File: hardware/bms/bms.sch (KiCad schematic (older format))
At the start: 159 parts

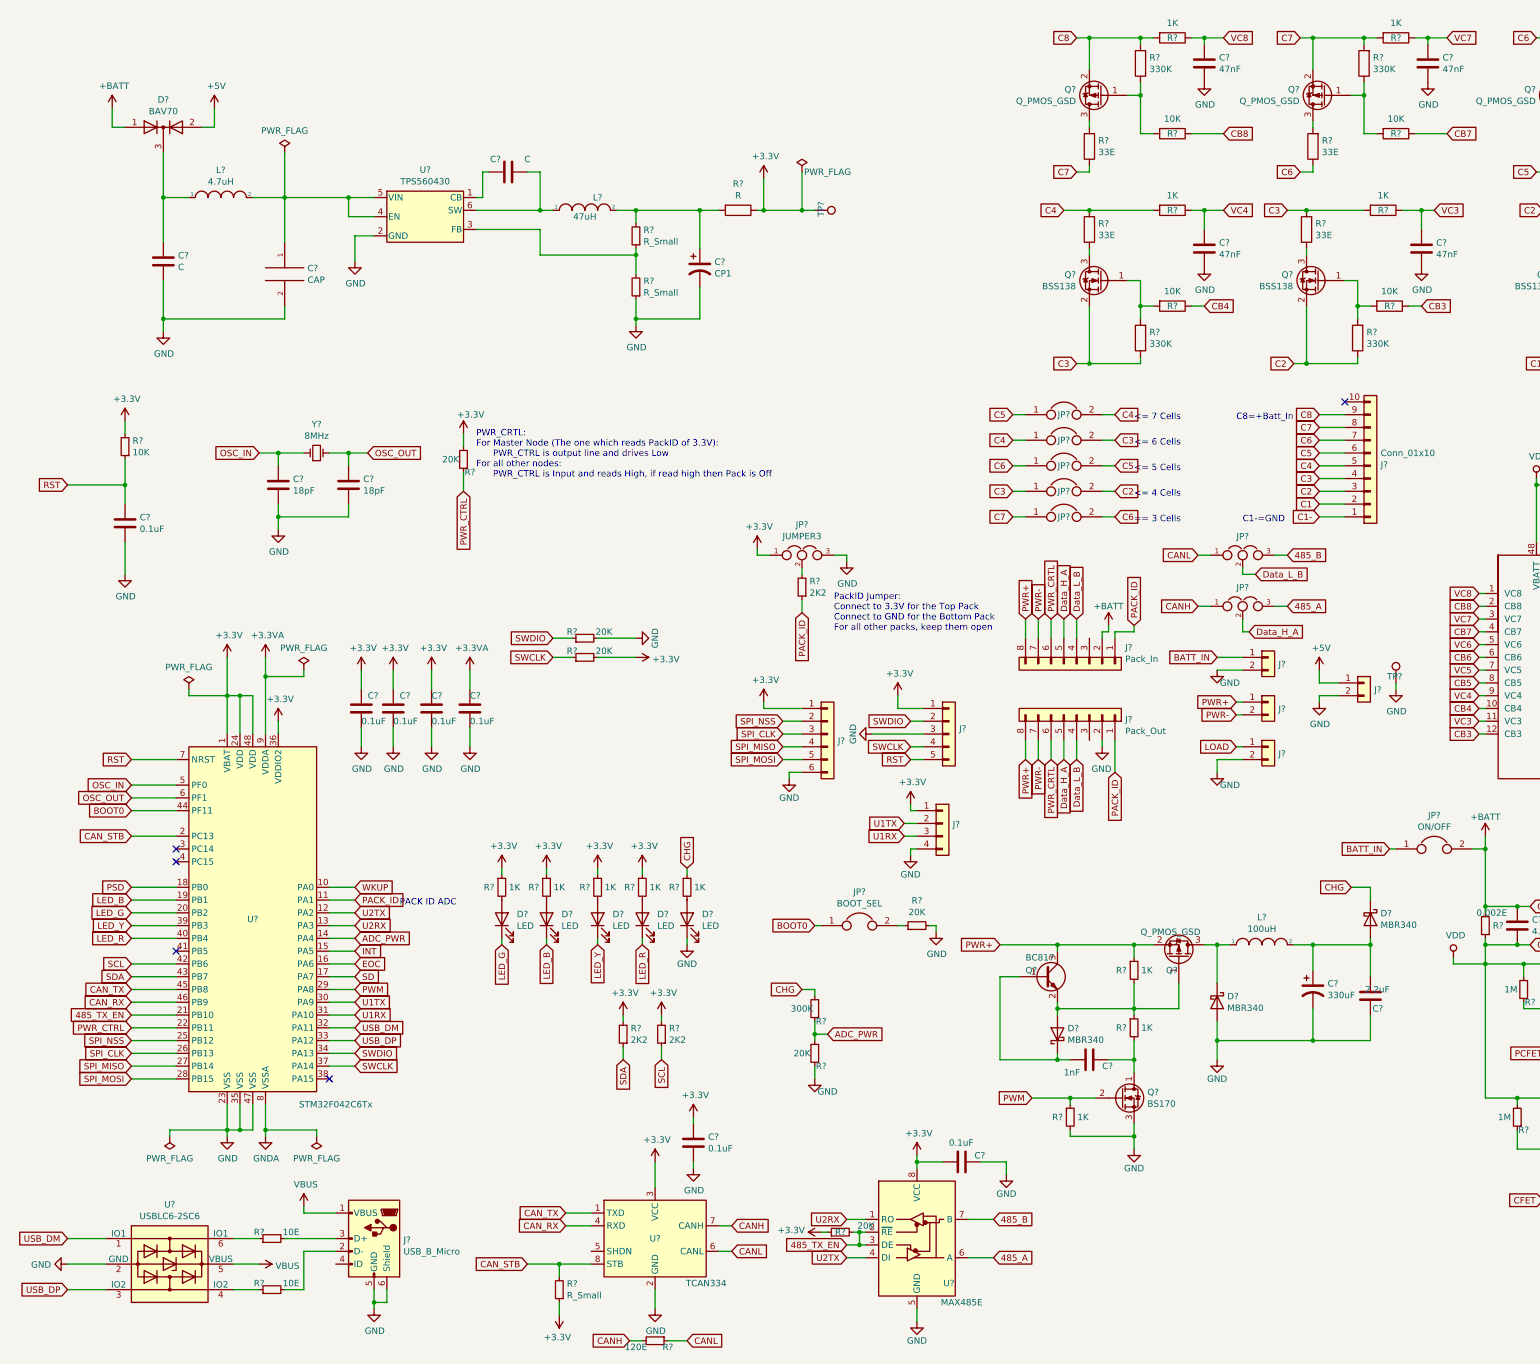
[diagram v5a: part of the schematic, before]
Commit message: added switching logic for gnd and chg control
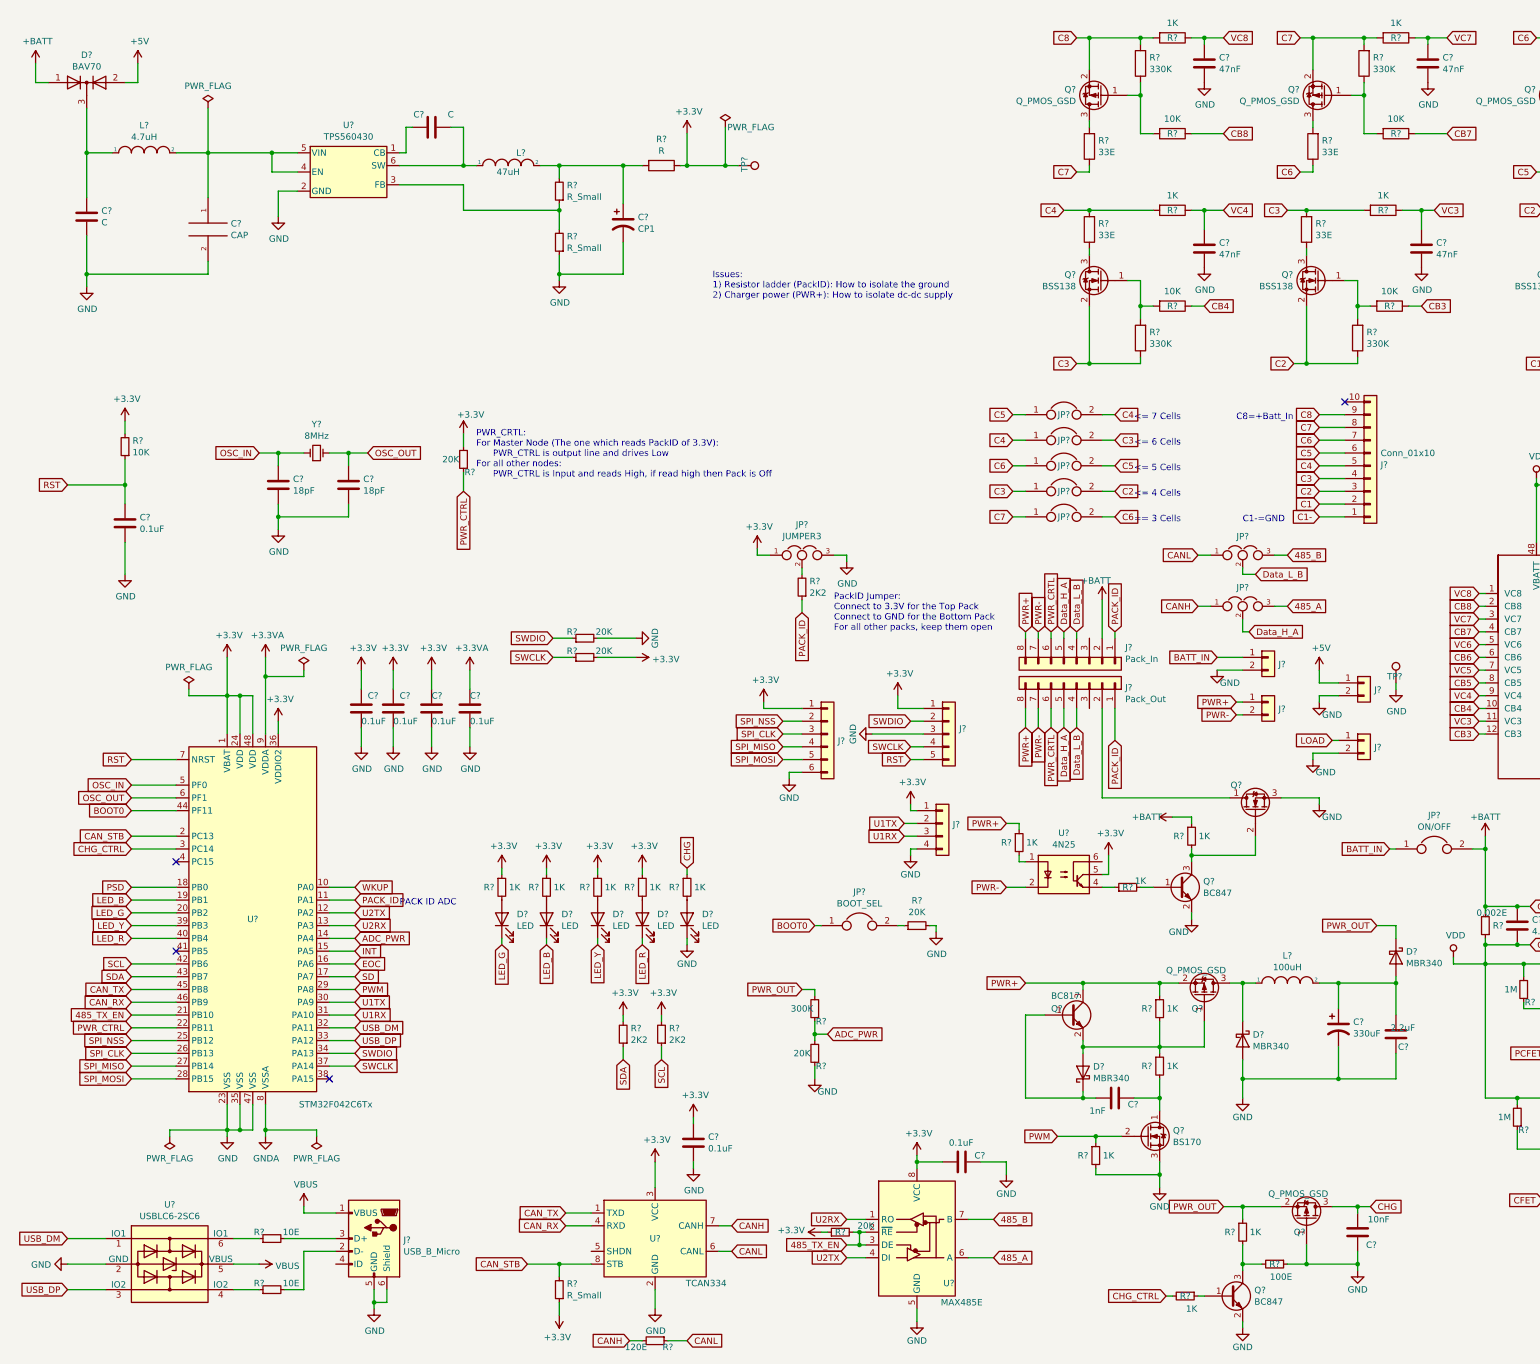
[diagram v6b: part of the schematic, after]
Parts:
- added C?: 10nF, Capacitor_SMD:C_0603_1608Metric_Pad1.05x0.95mm_HandSolder, symbol Device:C
- added Q?: Q_PMOS_GSD, symbol bms-rescue:Q_PMOS_GSD-BMS
- added Q? (x2): BC847, Package_TO_SOT_SMD:SOT-23, symbol Transistor_BJT:BC847
- added Q?: Q_NMOS_DGS, symbol Device:Q_NMOS_DGS
- added R? (x5): 1K, Resistor_SMD:R_0603_1608Metric_Pad1.05x0.95mm_HandSolder, symbol Device:R_Small
- added R?: 100E, Resistor_SMD:R_0603_1608Metric_Pad1.05x0.95mm_HandSolder, symbol Device:R_Small
- added U?: 4N25, Package_DIP:DIP-6_W7.62mm, symbol Isolator:4N25
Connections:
- net +3V3: now also U?.5
- net +BATT: now also R?.1
- net CHG: now also C?.2, Q?.3 (D); no longer D?.1 (K), R?.2
- net GND: now also C?.1, Q?.1 (G), Q?.2 (E), Q?.2 (E), Q?.3 (S), R?.1; no longer J?.2 (Pin_2)
- net PWR+: now also R?.1
- net PWR-: now also U?.2
- net CHG_CTRL: now reaches U?.3 (PC14)
- net CHG_CTRL: now also R?.2
- new net: Q?.1 (B), R?.1
- new net: Q?.3 (C), R?.2, R?.2
- new net: Q?.1 (B), R?.2
- new net: Q?.2 (G), Q?.3 (C), R?.2
- new net: R?.1, U?.4
- new net: J?.2 (Pin_2), Q?.1 (D)
- new net: R?.2, U?.1
- new net PWR_OUT: D?.1 (K), Q?.2 (S), R?.1, R?.2
- no-connect marks 7 -> 6
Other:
- note added: "Issues:\n1) Resistor ladder (PackID): How to isolate the ground\n2) Charger power (PWR+): How to isolate dc-dc supply"
- moved on the sheet: C?, D?, J?, L?, Q?, R?, TP?, U?

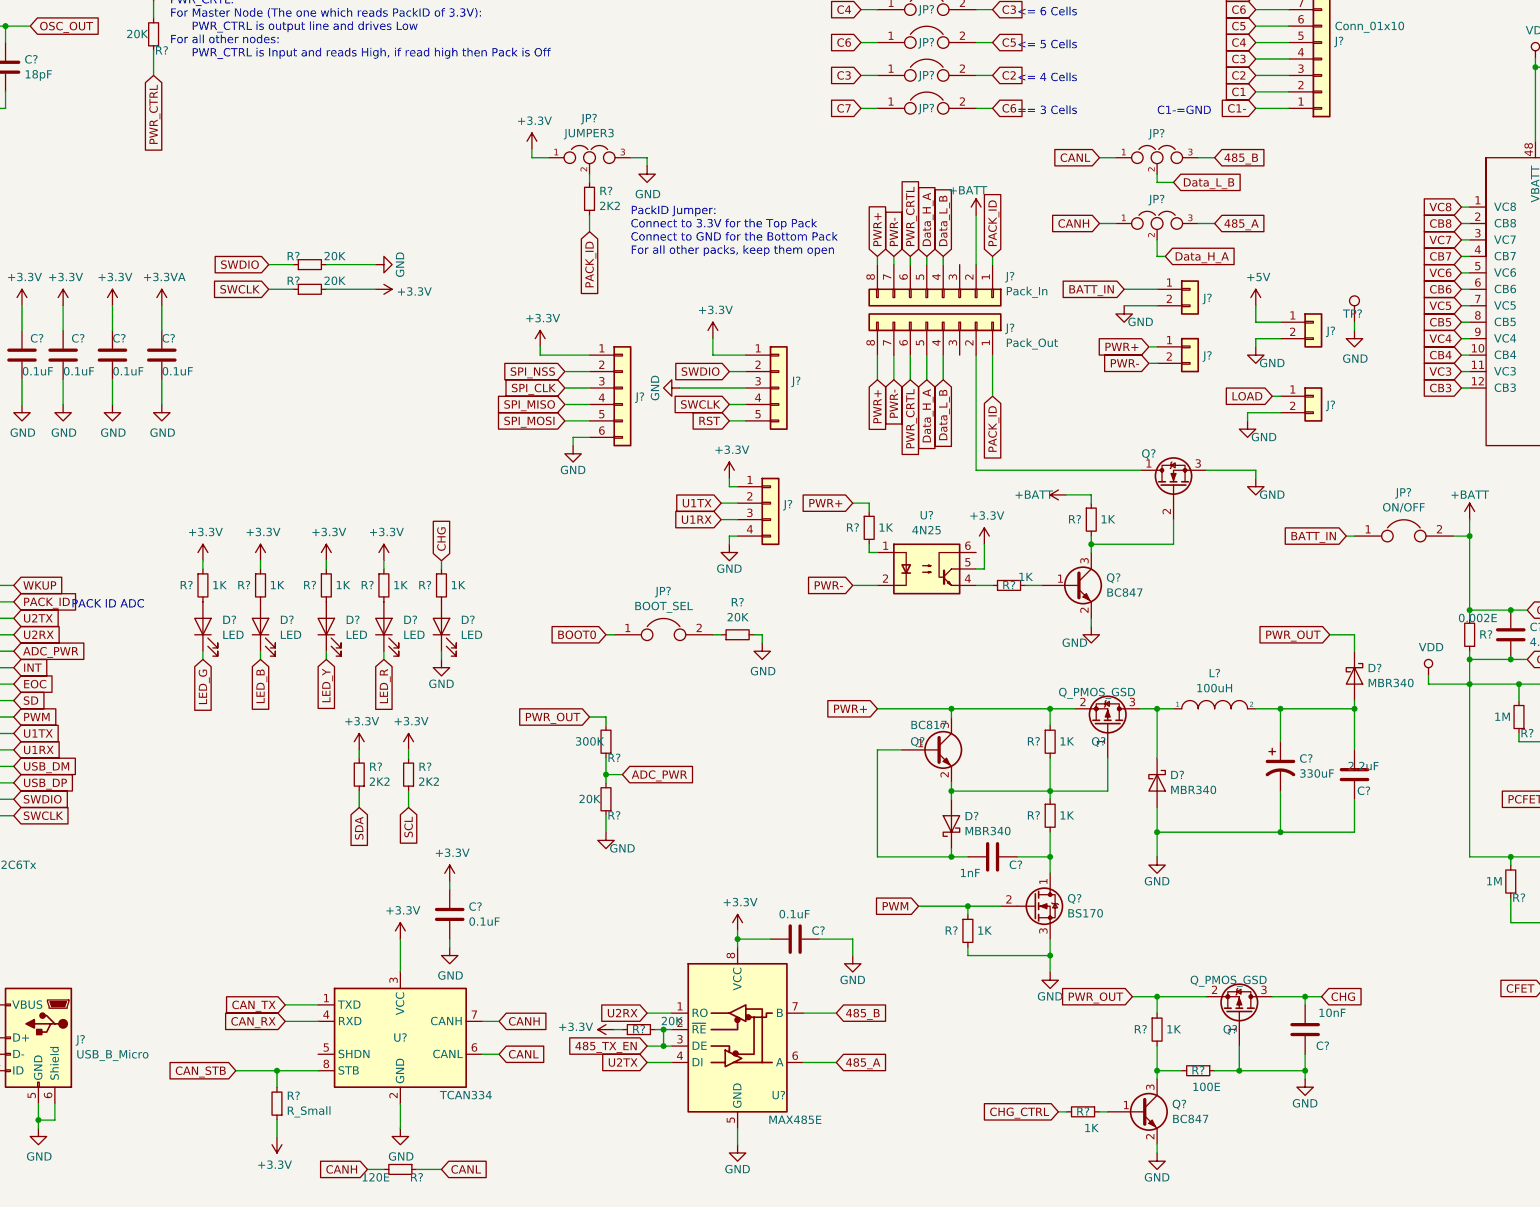
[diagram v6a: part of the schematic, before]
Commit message: updated charging logic and board to board connections
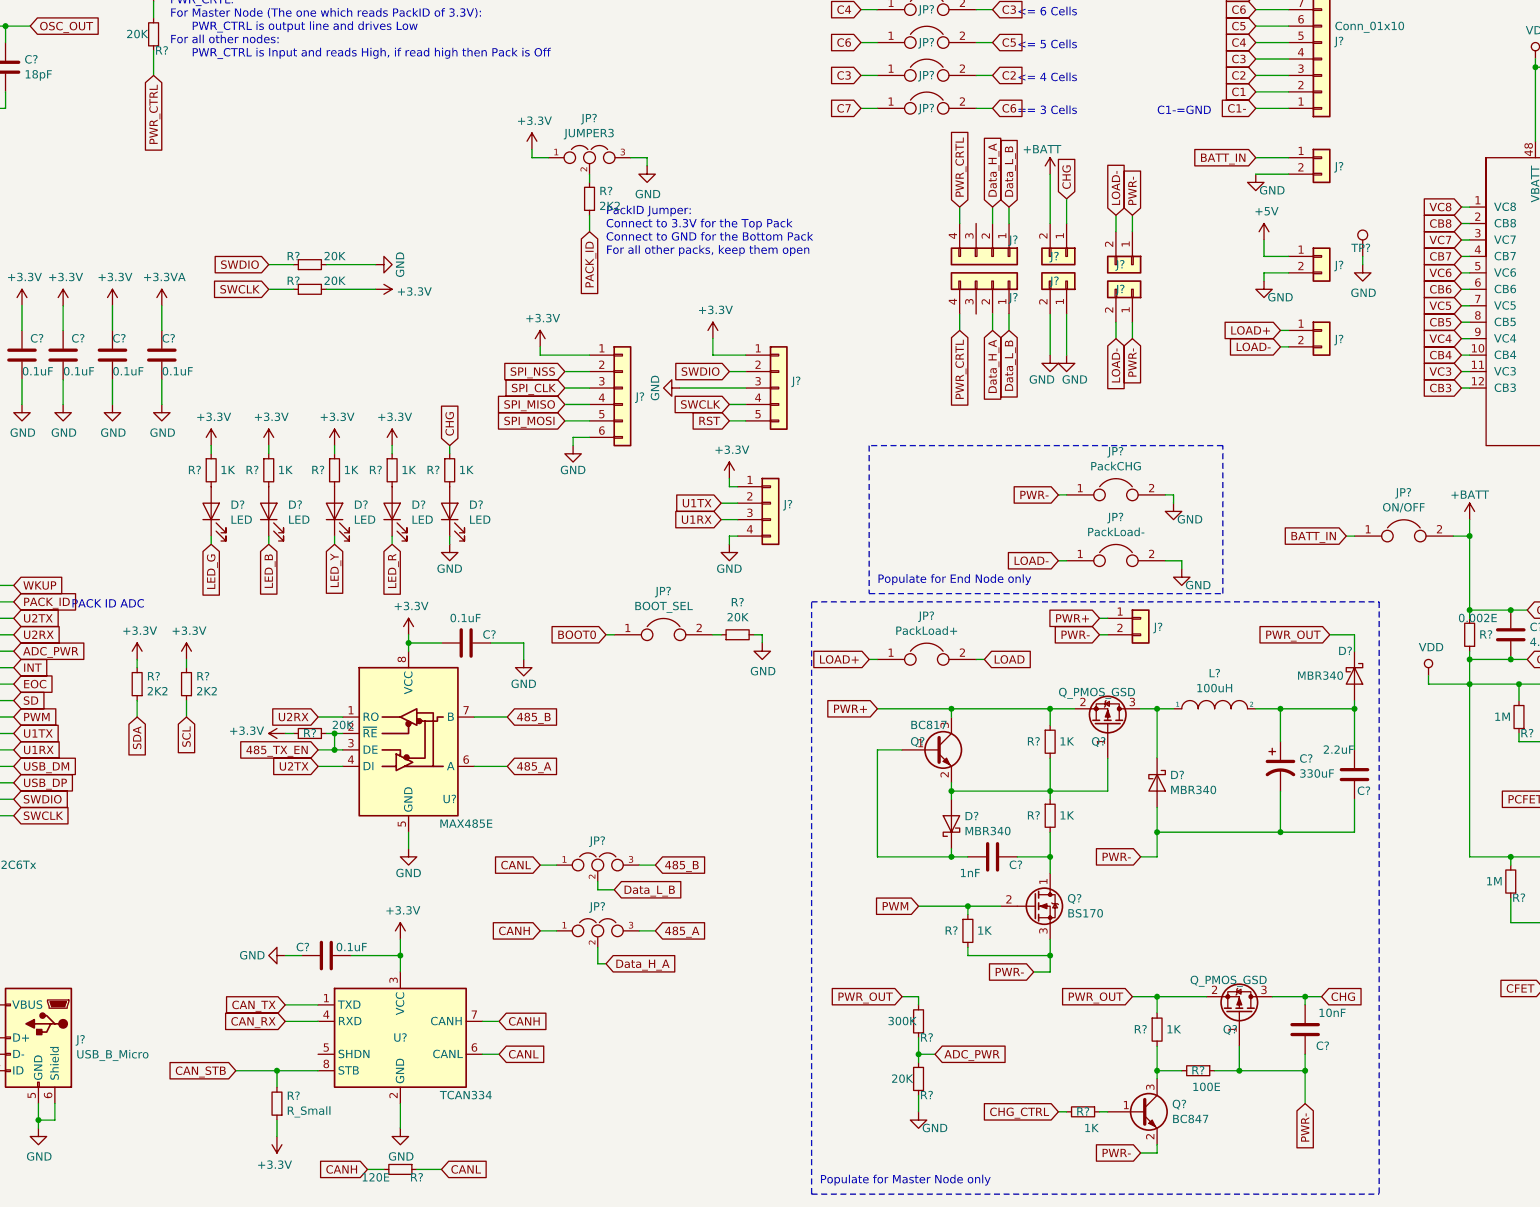
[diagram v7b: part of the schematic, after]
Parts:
- removed J?: Pack_In, symbol Connector_Generic:Conn_01x08
- removed J?: Pack_Out, symbol Connector_Generic:Conn_01x08
- removed Q?: BC847, Package_TO_SOT_SMD:SOT-23, symbol Transistor_BJT:BC847
- removed Q?: Q_NMOS_DGS, symbol Device:Q_NMOS_DGS
- removed R? (x3): 1K, Resistor_SMD:R_0603_1608Metric_Pad1.05x0.95mm_HandSolder, symbol Device:R_Small
- removed U?: 4N25, Package_DIP:DIP-6_W7.62mm, symbol Isolator:4N25
- added J? (x2): Conn_01x04, symbol Connector_Generic:Conn_01x04
- added J? (x4): Conn_01x02, symbol BMS:Conn_01x02
- added JP?: PackCHG, symbol BMS:JUMPER
- added JP?: PackLoad+, symbol BMS:JUMPER
- added JP?: PackLoad-, symbol BMS:JUMPER
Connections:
- net +3V3: now also C?.2; no longer C?.1
- net +BATT: now also J?.2 (Pin_2)
- net CHG: now also J?.1 (Pin_1)
- net Data_H_A: now also J?.2 (Pin_2), J?.2 (Pin_2)
- net Data_L_B: now also J?.1 (Pin_1), J?.1 (Pin_1)
- net GND: now also C?.1, J?.1 (Pin_1), J?.2 (Pin_2), JP?.2, JP?.2; no longer C?.1, C?.1, C?.2, C?.2, D?.2 (A), J?.2 (Pin_2), Q?.1 (G), Q?.2 (E), Q?.3 (S), R?.1, R?.2
- net LOAD: now also JP?.2; no longer J?.1 (Pin_1)
- net PWR-: now also C?.1, C?.1, C?.2, D?.2 (A), Q?.1 (G), Q?.2 (E), Q?.3 (S), R?.1, R?.2, J?.1 (Pin_1), J?.1 (Pin_1), JP?.1
- net PWR_CRTL: now also J?.4 (Pin_4), J?.4 (Pin_4)
- new net LOAD+: J?.1 (Pin_1), JP?.1
- new net LOAD-: J?.2 (Pin_2), J?.2 (Pin_2), J?.2 (Pin_2), JP?.1
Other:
- note added: "Populate for End Node only"
- note added: "Populate for Master Node only"
- moved on the sheet: C?, D?, J?, JP?, R?, TP?, U?
